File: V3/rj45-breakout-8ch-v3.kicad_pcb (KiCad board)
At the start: 2 copper layers, 93 x 67.8 mm, 16 parts, among them J1 Jack RJ45, J10 DB141V-2.54-6P, J11 DB141V-2.54-6P, J12 DB141V-2.54-6P, J13 DB141V-2.54-6P, J2 Jack RJ45, J3 Jack RJ45, J4 Jack RJ45, J5 Jack RJ45, J6 Jack RJ45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

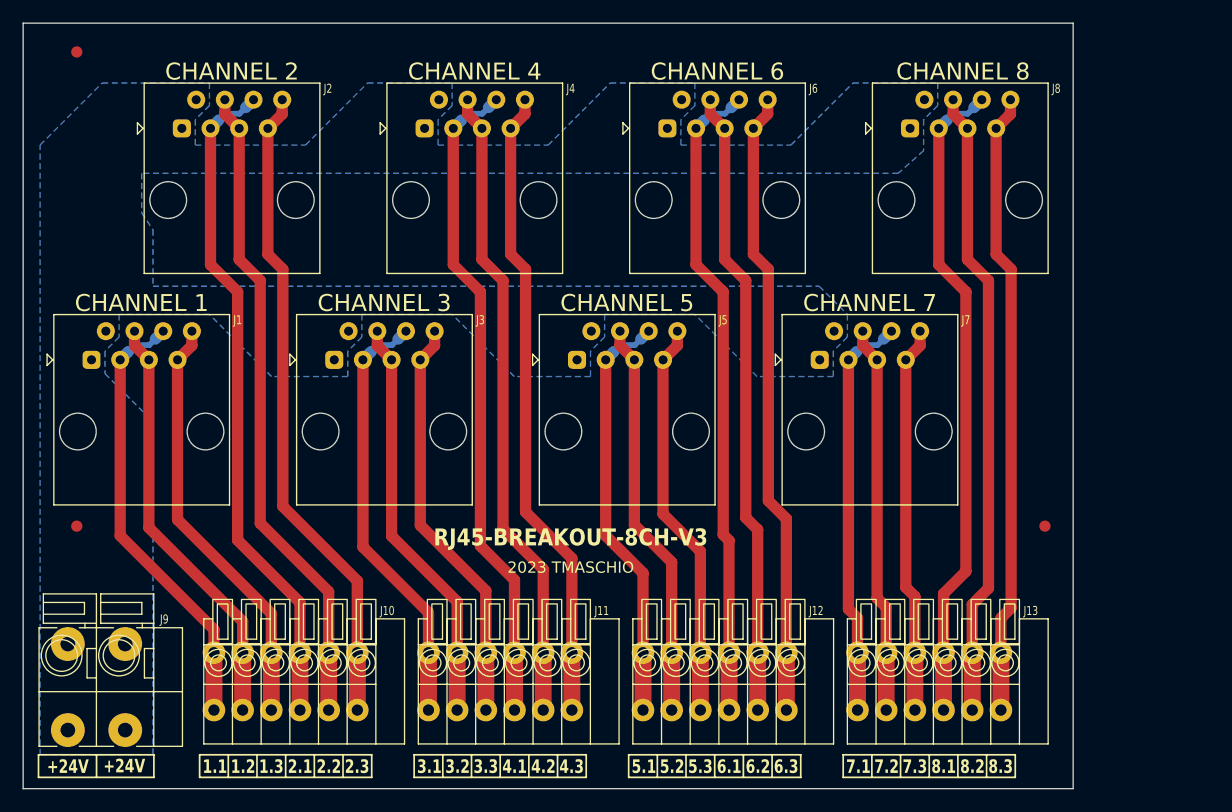
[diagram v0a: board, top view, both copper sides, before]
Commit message: Replaced 2.54mm pitch terminal blocks for 3.5mm pitch.
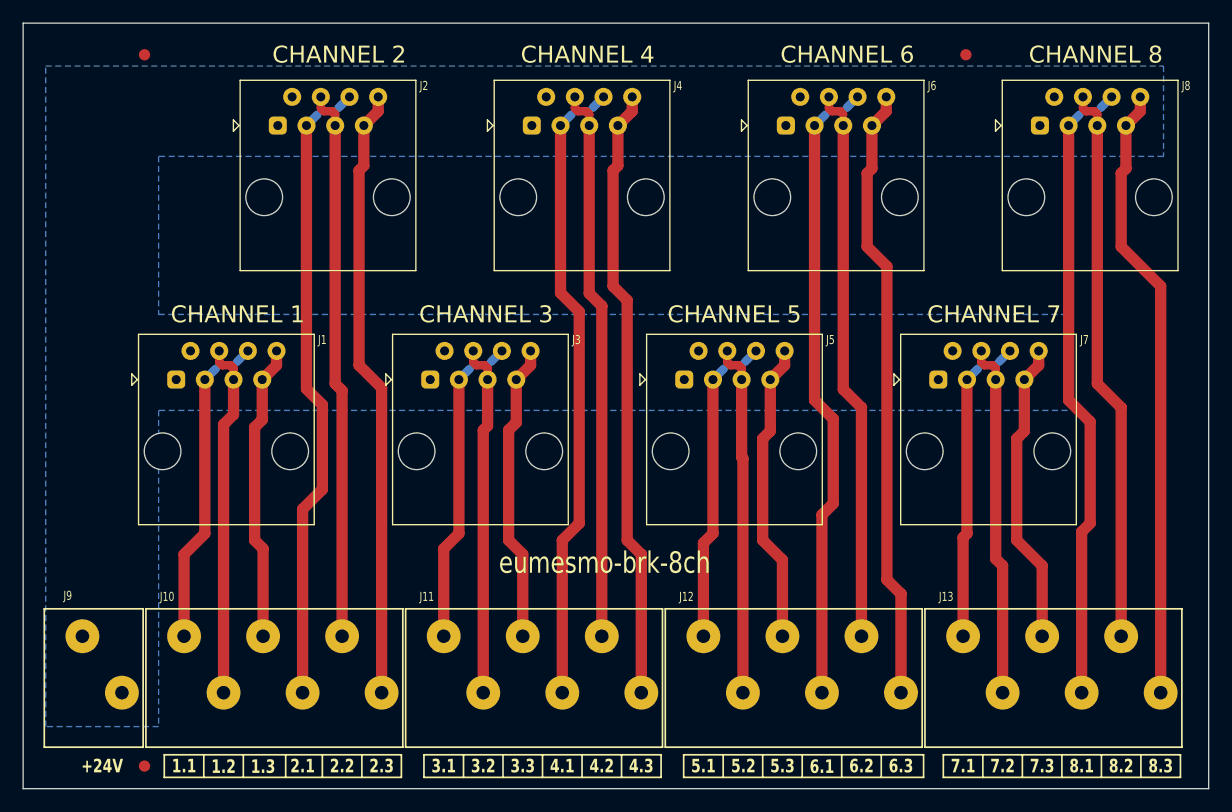
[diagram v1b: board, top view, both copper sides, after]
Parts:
- J10, J11, J12, J13: value DB141V-2.54-6P -> 250-206; footprint Tales:TerminalBlock_Dibo_DB141V-2.54-6P_1x06_P2.54mm_Vertical -> Tales:TerminalBlock_Wago_250-206_1x06_P3.5mm_45Degree
- J9: value DB142V-5.08-2P -> 250-202; footprint Tales:TerminalBlock_Dibo_DB142V-5.08-2P_1x02_P5.08mm_Vertical -> Tales:TerminalBlock_Wago_250-202_1x02_P3.5mm_45Degree
- moved FID3 42.3 mm to (183.5, 65.0)
- moved FID2 22.1 mm to (110.8, 128.0)
- moved J13 11.8 mm to (192.0, 119.0)
- moved J8 11.5 mm to (194.5, 70.0)
- moved J7 10.6 mm to (185.5, 92.5)
- moved J6 10.5 mm to (172.0, 70.0)
- moved J5 9.66 mm to (163.0, 92.5)
- moved J4 9.50 mm to (149.5, 70.0)
- moved J3 8.68 mm to (140.5, 92.5)
- moved J2 8.50 mm to (127.0, 70.0)
- moved J12 7.89 mm to (169.0, 119.0)
- moved J1 7.70 mm to (118.0, 92.5)
- moved FID1 6.01 mm to (110.8, 65.0)
- moved J11 4.04 mm to (146.0, 119.0)
- moved J9 2.06 mm to (107.0, 119.0)
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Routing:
- net /CH1PAR4: track 37.5 -> 26.4 mm
- net /CH1PAR2: track 39.3 -> 28.4 mm
- net /CH3PAR2: track 38.3 -> 28.1 mm
- net /CH3PAR4: track 36.5 -> 26.6 mm
- net /CH5PAR2: track 37.3 -> 27.9 mm
- net /CH2PAR3: track 57.9 -> 49.0 mm
- net /CH5PAR4: track 35.5 -> 26.8 mm
- net /CH7PAR2: track 36.2 -> 27.7 mm
- net /CH4PAR3: track 56.8 -> 49.2 mm
- net /CH7PAR4: track 34.4 -> 27.0 mm
- net /CH6PAR3: track 55.8 -> 49.4 mm
- net /CH8PAR3: track 56.0 -> 49.6 mm
- net /CH1PAR3: track 37.5 -> 31.6 mm
- net /CH3PAR3: track 36.5 -> 31.4 mm
- net /CH5PAR3: track 35.5 -> 31.3 mm
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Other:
- board size 93 x 67.8 mm -> 105 x 67.8 mm
- board text added: "eumesmo-brk-8ch"
- board text removed: "2023 TMASCHIO"
- board text removed: "RJ45-BREAKOUT-8CH-V3"
